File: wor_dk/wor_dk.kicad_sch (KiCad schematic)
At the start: 0 parts

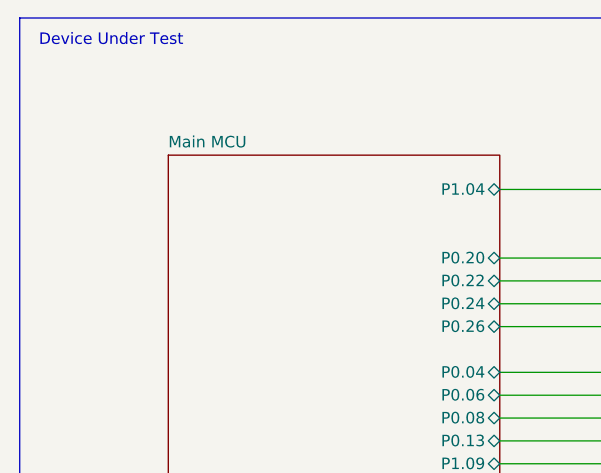
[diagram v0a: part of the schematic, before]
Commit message: wor_dk: adapt main MCU power supply to externally powered
The main MCU now has support for enabling DC/DC converter for REG1 as
per reference circuit configuration no. 5.
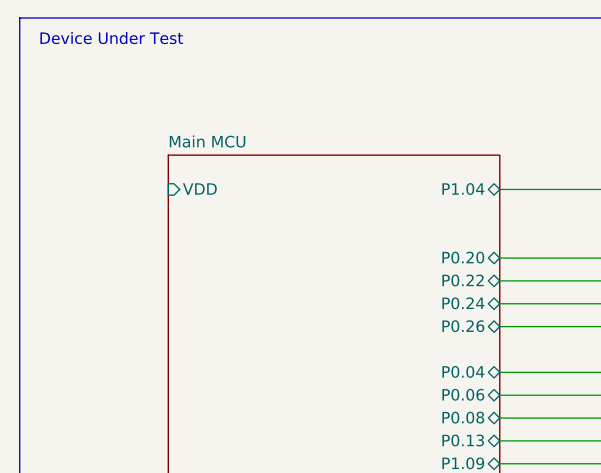
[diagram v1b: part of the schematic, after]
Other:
- sheet Main MCU ports: added VDD; removed none
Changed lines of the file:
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@@
+			)
+		)
+		(pin "VDD" input
+			(at 68.58 39.37 180)
+			(effects
+				(font
+					(size 1.27 1.27)
+				)
+				(justify left)
 			)
 		)

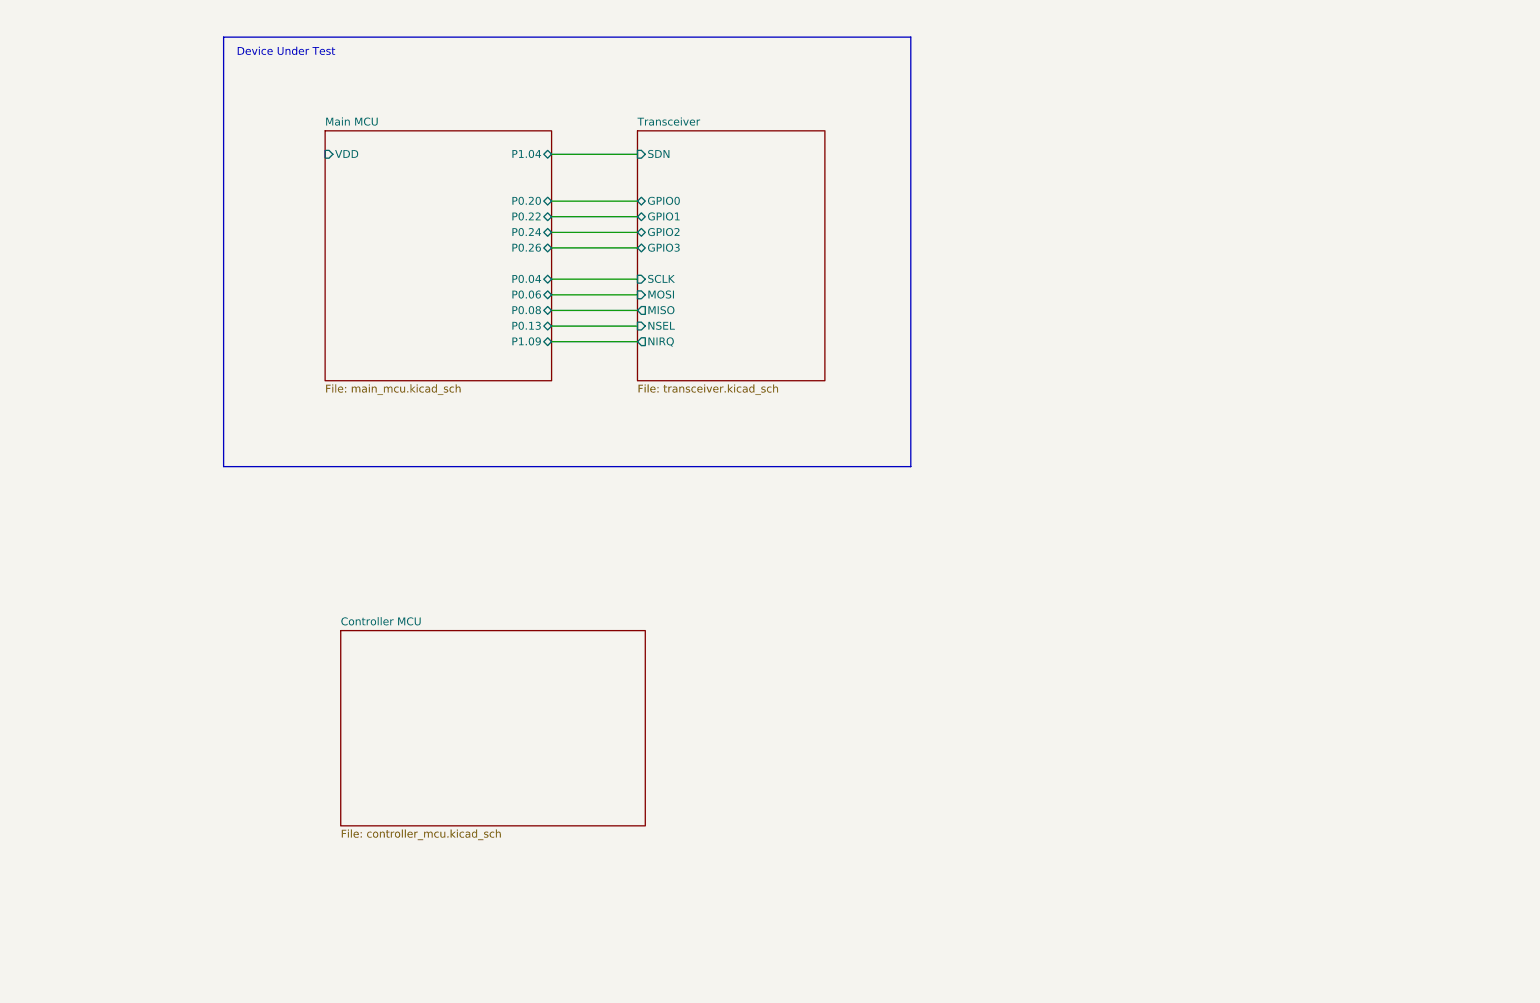
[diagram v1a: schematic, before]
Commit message: wor_dk: schematic: add multiplexers for programmer & GPIO
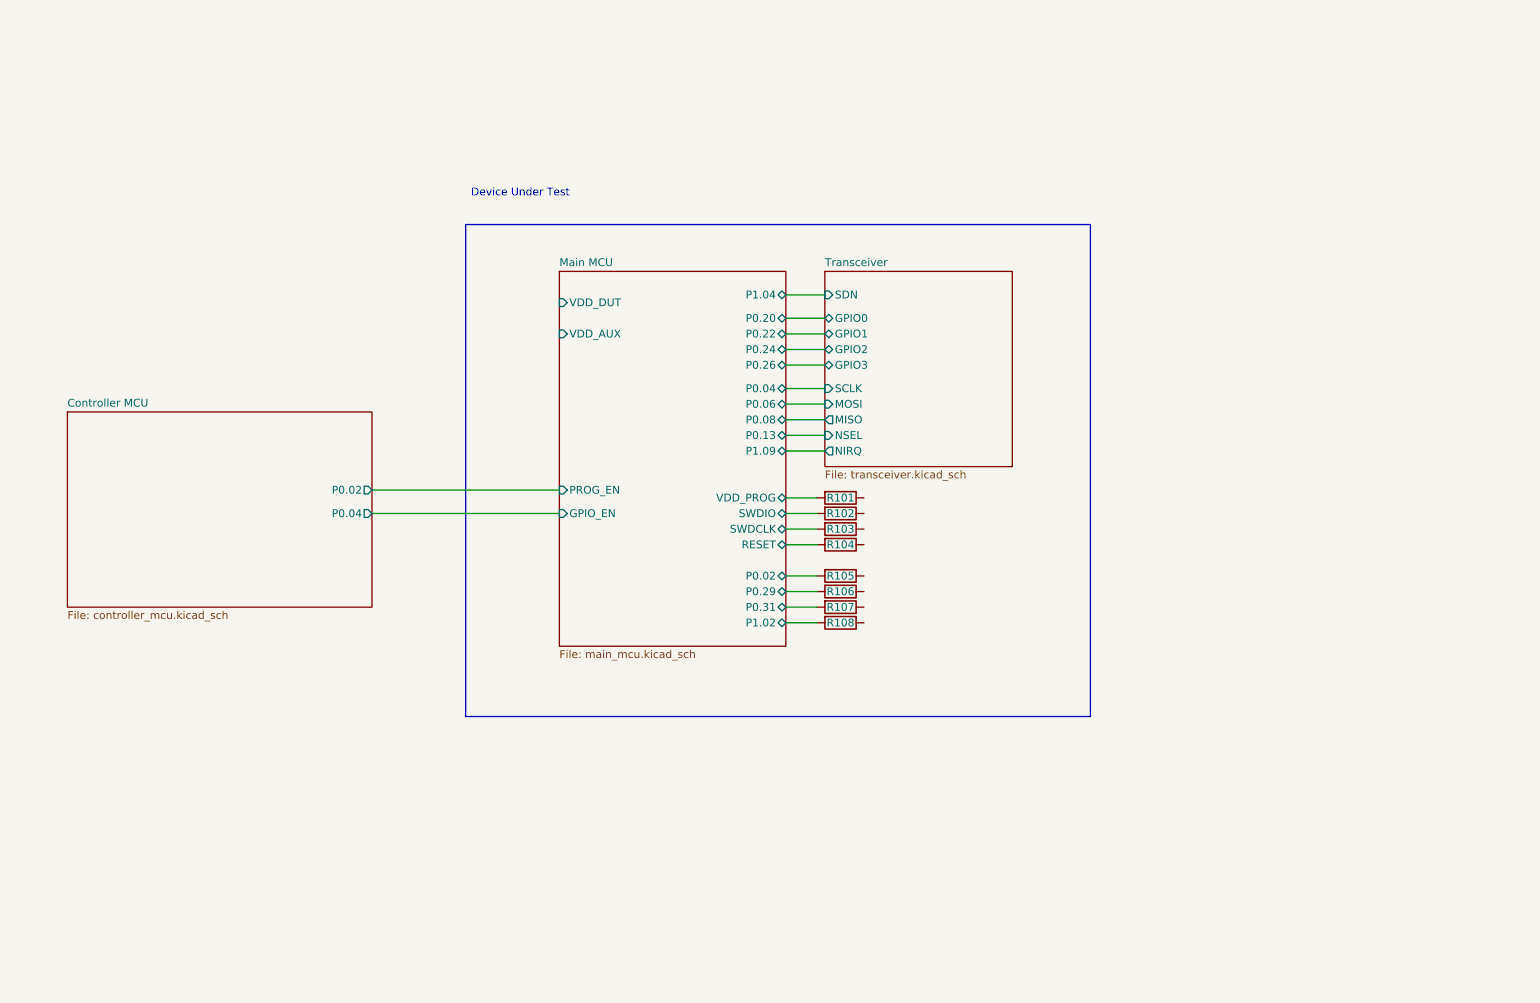
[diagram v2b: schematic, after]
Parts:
- added R101, R102, R103, R104, R105, R106, R107, R108: 0, symbol Device:R
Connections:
- new net Main MCU/P0.02: R105.2
- new net Main MCU/P0.29: R106.2
- new net Main MCU/P0.31: R107.2
- new net Main MCU/P1.02: R108.2
- new net Main MCU/RESET: R104.2
- new net Main MCU/SWDCLK: R103.2
- new net Main MCU/SWDIO: R102.2
- new net Main MCU/VDD_PROG: R101.2
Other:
- sheet Controller MCU ports: added P0.02, P0.04; removed none
- sheet Main MCU ports: added GPIO_EN, P0.02, P0.29, P0.31, P1.02, PROG_EN, RESET, SWDCLK, SWDIO, VDD_AUX, VDD_DUT, VDD_PROG; removed VDD

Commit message: wor_dk: schematic: add FT232RL
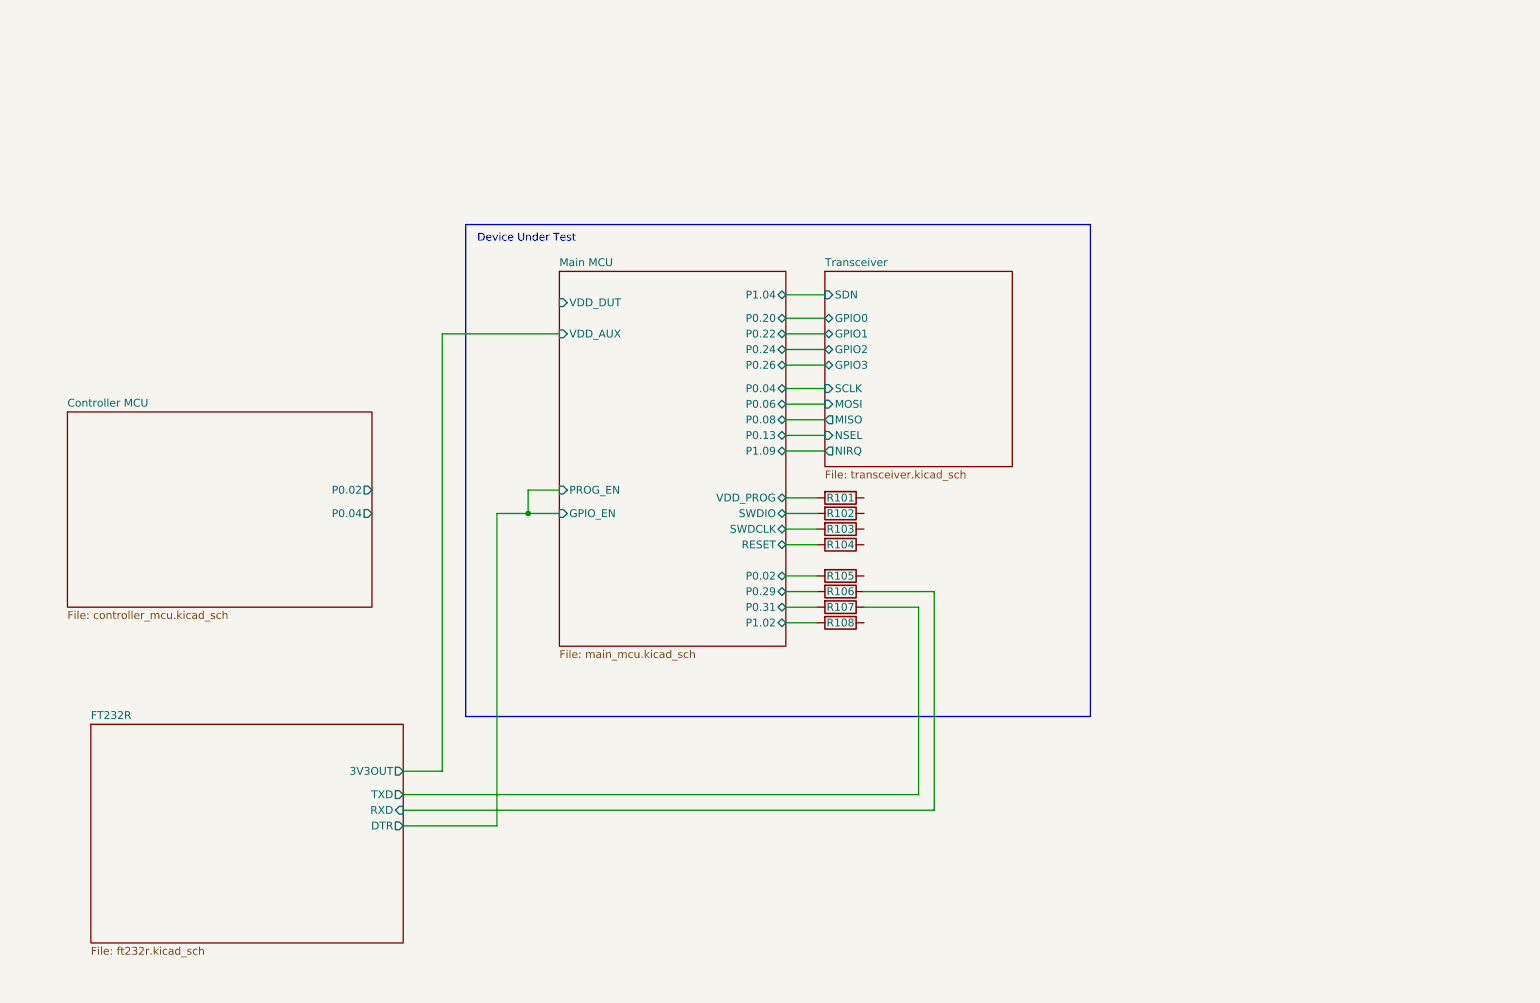
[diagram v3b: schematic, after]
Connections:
- net FT232R/TXD: now reaches R107.1
- net FT232R/RXD: now reaches R106.1
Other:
- added sheet FT232R (ft232r.kicad_sch)
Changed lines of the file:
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@@
 		(rev "0.1.0")
 	)
+	(junction
+		(at 101.6 97.79)
+		(diameter 0)
+		(color 0 0 0 0)
+	)
+	(wire
+		(pts
+			(xy 101.6 97.79) (xy 106.68 97.79)
+		)
+		(stroke
+			(width 0)
+			(type default)
+		)
+	)
+	(wire
+		(pts
+			(xy 101.6 93.98) (xy 101.6 97.79)
+		)
+		(stroke
+			(width 0)
+			(type default)
+		)
+	)
+	(wire
+		(pts
+			(xy 96.52 148.59) (xy 96.52 97.79)
+		)
+		(stroke
+			(width 0)
+			(type default)
+		)
+	)
 	(wire
 		(pts
@@
 	(wire
 		(pts
-			(xy 76.2 93.98) (xy 106.68 93.98)
+			(xy 81.28 143.51) (xy 165.1 143.51)
 		)
 		(stroke
@@
 	(wire
 		(pts
-			(xy 76.2 97.79) (xy 106.68 97.79)
+			(xy 167.64 110.49) (xy 156.21 110.49)
 		)
 		(stroke
@@
 	(wire
 		(pts
+			(xy 106.68 93.98) (xy 101.6 93.98)
+		)
+		(stroke
+			(width 0)
+			(type default)
+		)
+	)
+	(wire
+		(pts
 			(xy 143.51 107.95) (xy 148.59 107.95)
 		)
@@
 	(wire
 		(pts
+			(xy 165.1 143.51) (xy 165.1 113.03)
+		)
+		(stroke
+			(width 0)
+			(type default)
+		)
+	)
+	(wire
+		(pts
 			(xy 143.51 97.79) (xy 148.59 97.79)
 		)
@@
 	(wire
 		(pts
+			(xy 81.28 148.59) (xy 96.52 148.59)
+		)
+		(stroke
+			(width 0)
+			(type default)
+		)
+	)
+	(wire
+		(pts
+			(xy 96.52 97.79) (xy 101.6 97.79)
+		)
+		(stroke
+			(width 0)
+			(type default)
+		)
+	)
+	(wire
+		(pts
 			(xy 143.51 102.87) (xy 148.59 102.87)
 		)
@@
 	(wire
 		(pts
+			(xy 165.1 113.03) (xy 156.21 113.03)
+		)
+		(stroke
+			(width 0)
+			(type default)
+		)
+	)
+	(wire
+		(pts
 			(xy 143.51 68.58) (xy 149.86 68.58)
 		)
@@
 	(wire
 		(pts
+			(xy 81.28 139.7) (xy 87.63 139.7)
+		)
+		(stroke
+			(width 0)
+			(type default)
+		)
+	)
+	(wire
+		(pts
 			(xy 143.51 113.03) (xy 148.59 113.03)
 		)
@@
 	(wire
 		(pts
+			(xy 87.63 139.7) (xy 87.63 68.58)
+		)
+		(stroke
+			(width 0)
+			(type default)
+		)
+	)
+	(wire
+		(pts
 			(xy 143.51 77.47) (xy 149.86 77.47)
 		)
@@
 	(wire
 		(pts
+			(xy 87.63 68.58) (xy 106.68 68.58)
+		)
+		(stroke
+			(width 0)
+			(type default)
+		)
+	)
+	(wire
+		(pts
+			(xy 81.28 146.05) (xy 167.64 146.05)
+		)
+		(stroke
+			(width 0)
+			(type default)
+		)
+	)
+	(wire
+		(pts
 			(xy 143.51 71.12) (xy 149.86 71.12)
+		)
+		(stroke
+			(width 0)
+			(type default)
+		)
+	)
+	(wire
+		(pts
+			(xy 167.64 146.05) (xy 167.64 110.49)
 		)
 		(stroke
@@
 	(text "Device Under Test"
 		(exclude_from_sim no)
-		(at 100.33 45.72 0)
+		(at 101.346 53.086 0)
 		(effects
 			(font
@@
 				)
 			)
+		)
+	)
+	(sheet
+		(at 30.48 132.08)
+		(size 50.8 35.56)
+		(fields_autoplaced yes)
+		(stroke
+			(width 0.1524)
+			(type solid)
+		)
+		(fill
+			(color 0 0 0 0.0000)
+		)
+		(property "Sheetname" "FT232R"
+			(at 30.48 131.3684 0)
+			(effects
+				(font
+					(size 1.27 1.27)
+				)
+				(justify left bottom)
+			)
+		)
+		(property "Sheetfile" "ft232r.kicad_sch"
+			(at 30.48 168.2246 0)
+			(effects
+				(font
+					(size 1.27 1.27)
+				)
+				(justify left top)
+			)
+		)
+		(pin "3V3OUT" output
+			(at 81.28 139.7 0)
+			(effects
+				(font
+					(size 1.27 1.27)
+				)
+				(justify right)
+			)
+		)
+		(pin "TXD" output
+			(at 81.28 143.51 0)
+			(effects
+				(font
+					(size 1.27 1.27)
+				)
+				(justify right)
+			)
+		)
+		(pin "RXD" input
+			(at 81.28 146.05 0)
+			(effects
+				(font
+					(size 1.27 1.27)
+				)
+				(justify right)
+			)
+		)
+		(pin "DTR" output
+			(at 81.28 148.59 0)
+			(effects
+				(font
+					(size 1.27 1.27)
+				)
+				(justify right)
+			)
+		)
+		(instances
+			(project "wor_dk"
+				(path "/8d3147eb-060b-4f65-bf42-ed06a58b21ba"
+					(page "5")
+				)
+			)

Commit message: wor_dk: add programmer
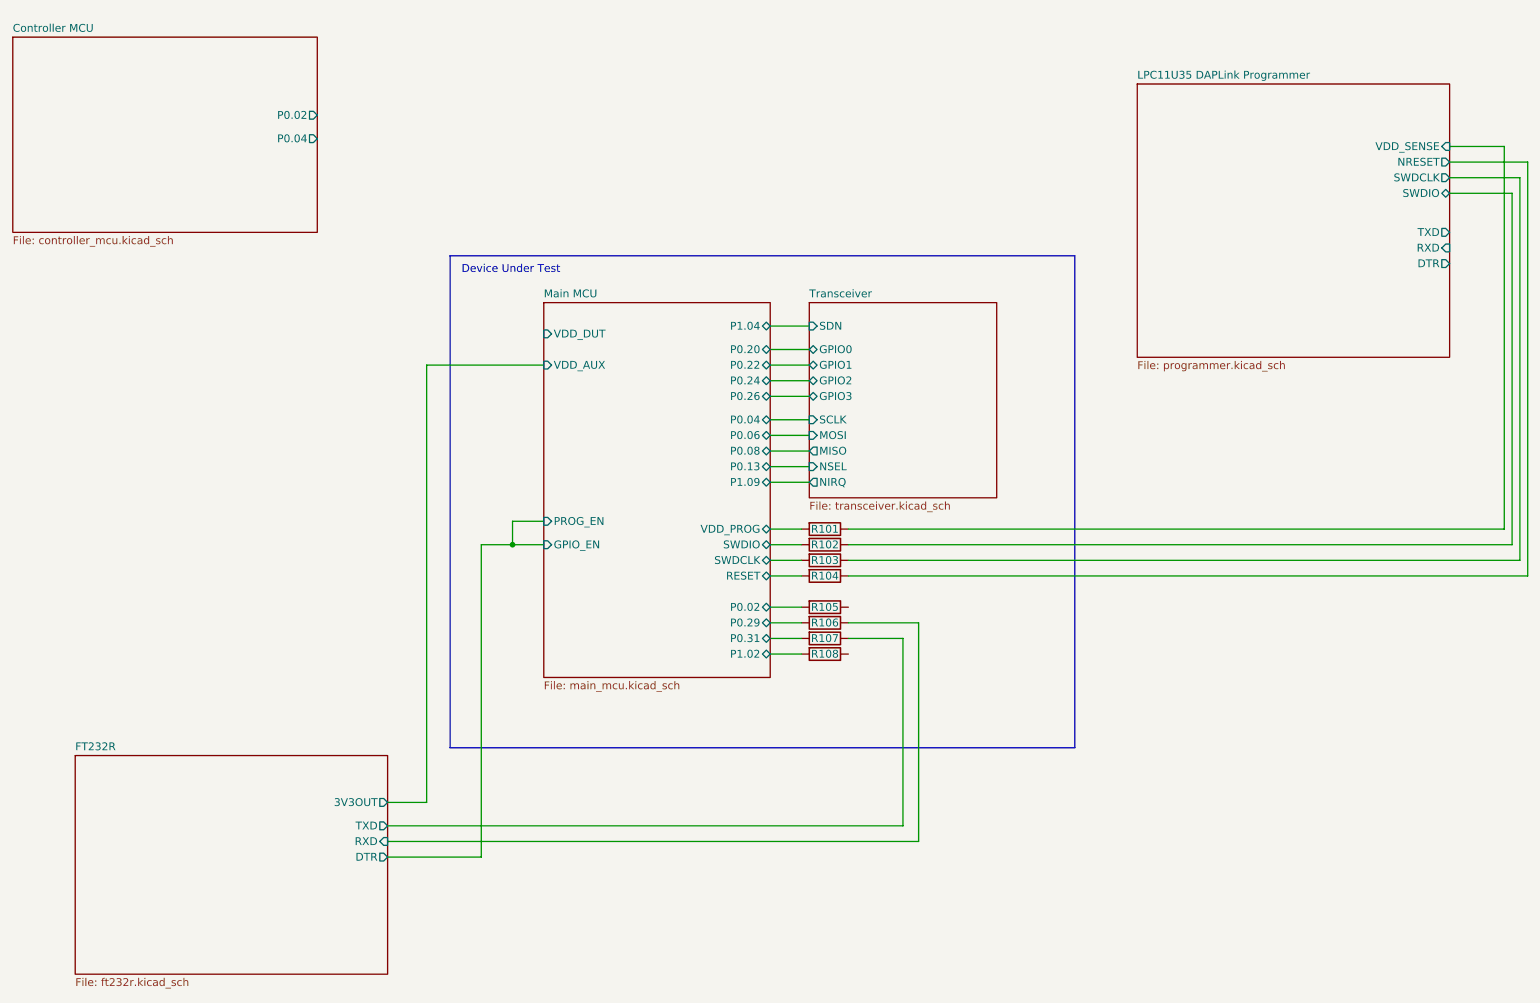
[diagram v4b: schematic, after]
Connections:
- net LPC11U35 DAPLink Programmer/NRESET: now reaches R104.1
- net LPC11U35 DAPLink Programmer/SWDIO: now reaches R102.1
- net LPC11U35 DAPLink Programmer/SWDCLK: now reaches R103.1
- net LPC11U35 DAPLink Programmer/VDD_SENSE: now reaches R101.1
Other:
- added sheet LPC11U35 DAPLink Programmer (programmer.kicad_sch)
- moved on the sheet: R101, R102, R103, R104, R105, R106, R107, R108
